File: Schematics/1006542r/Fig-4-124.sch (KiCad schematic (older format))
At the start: 15 parts, among them J1 ConnectorGeneric, U601 D3NOR-+3VDC-0VDC-nd1021041-A_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, U602 D3NOR-+3VDC-0VDC-nd1021041-AB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, U603 D3NOR-+3VDC-0VDC-nd1021041-AB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, U604 D3NOR-+3VDC-0VDC-nd1021041-AB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, U605 D3NOR-+3VDC-0VDC-nd1021041-_B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, U606 D3NOR-+3VDC-0VDC-nd1021041-_B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, U607 D3NOR-+3VDC-0VDC-nd1021041-_B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, U608 D3NOR-+3VDC-0VDC-nd1021041-_B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, U609 D3NOR-+3VDC-0VDC-nd1021041-_B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, U610 D3NOR-+3VDC-0VDC-nd1021041-A_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, U611 D3NOR-+3VDC-0VDC-nd1021041-_B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, U612 D3NOR-NC-0VDC-expander-nd1021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, U613 D3NOR-+3VDC-0VDC-nd1021041-_B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, U614 D3NOR-+3VDC-0VDC-nd1021041-_B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

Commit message: When I started recovering transcribed Block I schematics from document ND-1021041, there was no info available to me on the pinout of the NOR-gates they used, and it didn't occur to me that any might be forthcoming, so I chose a pinout arbitrarily.  It turns out that we now have the required info (SCD 1006771), and my arbitrary choices were wrong. I've therefore updated the NOR-library generator script, the relevant NOR libraries themselves, and all of the so-far-recovered Block I schematics using those gates.  It doesn't really matter in the cosmic sense, since the real Block I schematics have become available in the meantime, so that these recovered schematics are of less interest, but it will come in handy when I eventually want to do cross-checking.  I haven't checked these updated schematics in full detail, but I've spot-checked them, and run some ERCs and netlists, and it looks good to me.
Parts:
- U601, U610: value D3NOR-+3VDC-0VDC-nd1021041-A_C-___ -> D3NOR-+3VDC-0VDC-nd1021041-1_5-___; symbol D3NOR-+3VDC-0VDC-nd1021041:D3NOR-+3VDC-0VDC-nd1021041-A_C-___ -> D3NOR-+3VDC-0VDC-nd1021041:D3NOR-+3VDC-0VDC-nd1021041-1_5-___
- U602, U603, U604: value D3NOR-+3VDC-0VDC-nd1021041-ABC-___ -> D3NOR-+3VDC-0VDC-nd1021041-135-___; symbol D3NOR-+3VDC-0VDC-nd1021041:D3NOR-+3VDC-0VDC-nd1021041-ABC-___ -> D3NOR-+3VDC-0VDC-nd1021041:D3NOR-+3VDC-0VDC-nd1021041-135-___
- U605, U606, U607, U608, U609, U611, U613, U614: value D3NOR-+3VDC-0VDC-nd1021041-_B_-___ -> D3NOR-+3VDC-0VDC-nd1021041-_3_-___; symbol D3NOR-+3VDC-0VDC-nd1021041:D3NOR-+3VDC-0VDC-nd1021041-_B_-___ -> D3NOR-+3VDC-0VDC-nd1021041:D3NOR-+3VDC-0VDC-nd1021041-_3_-___
- U612: value D3NOR-NC-0VDC-expander-nd1021041-A_C-___ -> D3NOR-NC-0VDC-expander-nd1021041-1_5-___; symbol D3NOR-NC-0VDC-expander-nd1021041:D3NOR-NC-0VDC-expander-nd1021041-A_C-___ -> D3NOR-NC-0VDC-expander-nd1021041:D3NOR-NC-0VDC-expander-nd1021041-1_5-___
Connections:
- net +3VDC: now also U601.8 (+3VDC), U602.8 (+3VDC), U603.8 (+3VDC), U604.8 (+3VDC), U605.8 (+3VDC), U606.8 (+3VDC), U607.8 (+3VDC), U608.8 (+3VDC), U609.8 (+3VDC), U610.8 (+3VDC), U611.8 (+3VDC), U613.8 (+3VDC), U614.8 (+3VDC); no longer U601.6 (+3VDC), U602.6 (+3VDC), U603.6 (+3VDC), U604.6 (+3VDC), U605.6 (+3VDC), U606.6 (+3VDC), U607.6 (+3VDC), U608.6 (+3VDC), U609.6 (+3VDC), U610.6 (+3VDC), U611.6 (+3VDC), U613.6 (+3VDC), U614.6 (+3VDC)
- net 0VDC: now also U601.4 (0VDC), U602.4 (0VDC), U603.4 (0VDC), U604.4 (0VDC), U605.1 (0VDC), U606.1 (0VDC), U607.1 (0VDC), U608.1 (0VDC), U609.1 (0VDC), U610.4 (0VDC), U611.1 (0VDC), U612.4 (0VDC), U613.1 (0VDC), U614.1 (0VDC); no longer U601.5 (0VDC), U602.5 (0VDC), U603.5 (0VDC), U604.5 (0VDC), U605.2 (0VDC), U606.2 (0VDC), U607.2 (0VDC), U608.2 (0VDC), U609.2 (0VDC), U610.5 (0VDC), U611.2 (0VDC), U612.5 (0VDC), U613.2 (0VDC), U614.2 (0VDC)
- net PIN51: now also U602.1; no longer U602.4 (A)
- net PIN57: now also U612.5; no longer U612.2 (C)
- net PIN63: now also U610.5; no longer U610.2 (C)
- net at J1.49: now also U611.7; no longer U611.1 (J)
- net at J1.69: now also U601.1; no longer U601.4 (A)
- net at J1.55: now also U609.7; no longer U609.1 (J)
- net at U604.1: now also J1.61, U602.5, U603.5, U610.1; no longer U609.3 (B)
- net at U605.3: now also U602.7; no longer U602.1 (J)
- net at U611.3, U613.3, U614.3: now also U605.7; no longer U605.1 (J)
- net at J1.59: now also U608.7; no longer U608.1 (J)
- net at J1.73: now also U603.1; no longer U603.4 (A)
- net at J1.75: now also U601.5; no longer U601.2 (C)
- net at U606.3, U607.3, U608.3: now also U603.7; no longer U603.1 (J)
- new net: J1.83, U606.7, U607.7
- new net: J1.43, U613.7, U614.7
- new net: U604.7, U609.3
- new net: J1.53, U610.7, U612.7
- new net: U601.7, U604.5, U612.1
- now unconnected: U602.2 (C), U603.2 (C), U604.2 (C)
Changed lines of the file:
@@
 $EndComp
 $Comp
-L D3NOR-+3VDC-0VDC-nd1021041:D3NOR-+3VDC-0VDC-nd1021041-_B_-___ U609
+L D3NOR-+3VDC-0VDC-nd1021041:D3NOR-+3VDC-0VDC-nd1021041-_3_-___ U609
 U 1 1 5BF978FA
 P 13050 7300
 F 0 "U609" H 13050 7625 140 0001 C CNB
-F 1 "D3NOR-+3VDC-0VDC-nd1021041-_B_-___" H 13050 7725 140 0001 C CNN
+F 1 "D3NOR-+3VDC-0VDC-nd1021041-_3_-___" H 13050 7725 140 0001 C CNN
 F 2 "" H 13050 7775 140 0001 C CNN
 F 3 "" H 13050 7775 140 0001 C CNN
@@
 $EndComp
 $Comp
-L D3NOR-+3VDC-0VDC-nd1021041:D3NOR-+3VDC-0VDC-nd1021041-A_C-___ U610
+L D3NOR-+3VDC-0VDC-nd1021041:D3NOR-+3VDC-0VDC-nd1021041-1_5-___ U610
 U 1 1 5BF978FB
 P 13050 8500
 F 0 "U610" H 13050 8825 140 0001 C CNB
-F 1 "D3NOR-+3VDC-0VDC-nd1021041-A_C-___" H 13050 8925 140 0001 C CNN
+F 1 "D3NOR-+3VDC-0VDC-nd1021041-1_5-___" H 13050 8925 140 0001 C CNN
 F 2 "" H 13050 8975 140 0001 C CNN
 F 3 "" H 13050 8975 140 0001 C CNN
@@
 $EndComp
 $Comp
-L D3NOR-NC-0VDC-expander-nd1021041:D3NOR-NC-0VDC-expander-nd1021041-A_C-___ U612
+L D3NOR-NC-0VDC-expander-nd1021041:D3NOR-NC-0VDC-expander-nd1021041-1_5-___ U612
 U 1 1 5BF978FC
 P 13100 9500
 F 0 "U612" H 13100 9825 140 0001 C CNB
-F 1 "D3NOR-NC-0VDC-expander-nd1021041-A_C-___" H 13100 9925 140 0001 C CNN
+F 1 "D3NOR-NC-0VDC-expander-nd1021041-1_5-___" H 13100 9925 140 0001 C CNN
 F 2 "" H 13100 9975 140 0001 C CNN
 F 3 "" H 13100 9975 140 0001 C CNN
@@
 $EndComp
 $Comp
-L D3NOR-+3VDC-0VDC-nd1021041:D3NOR-+3VDC-0VDC-nd1021041-ABC-___ U602
+L D3NOR-+3VDC-0VDC-nd1021041:D3NOR-+3VDC-0VDC-nd1021041-135-___ U602
 U 1 1 5BF978FD
 P 7350 11675
 F 0 "U602" H 7350 12000 140 0001 C CNB
-F 1 "D3NOR-+3VDC-0VDC-nd1021041-ABC-___" H 7350 12100 140 0001 C CNN
+F 1 "D3NOR-+3VDC-0VDC-nd1021041-135-___" H 7350 12100 140 0001 C CNN
 F 2 "" H 7350 12150 140 0001 C CNN
 F 3 "" H 7350 12150 140 0001 C CNN
@@
 $EndComp
 $Comp
-L D3NOR-+3VDC-0VDC-nd1021041:D3NOR-+3VDC-0VDC-nd1021041-_B_-___ U605
+L D3NOR-+3VDC-0VDC-nd1021041:D3NOR-+3VDC-0VDC-nd1021041-_3_-___ U605
 U 1 1 5BF978FE
 P 10225 11675
 F 0 "U605" H 10225 12000 140 0001 C CNB
-F 1 "D3NOR-+3VDC-0VDC-nd1021041-_B_-___" H 10225 12100 140 0001 C CNN
+F 1 "D3NOR-+3VDC-0VDC-nd1021041-_3_-___" H 10225 12100 140 0001 C CNN
 F 2 "" H 10225 12150 140 0001 C CNN
 F 3 "" H 10225 12150 140 0001 C CNN
@@
 $EndComp
 $Comp
-L D3NOR-+3VDC-0VDC-nd1021041:D3NOR-+3VDC-0VDC-nd1021041-_B_-___ U611
+L D3NOR-+3VDC-0VDC-nd1021041:D3NOR-+3VDC-0VDC-nd1021041-_3_-___ U611
 U 1 1 5BF978FF
 P 13075 10475
 F 0 "U611" H 13075 10800 140 0001 C CNB
-F 1 "D3NOR-+3VDC-0VDC-nd1021041-_B_-___" H 13075 10900 140 0001 C CNN
+F 1 "D3NOR-+3VDC-0VDC-nd1021041-_3_-___" H 13075 10900 140 0001 C CNN
 F 2 "" H 13075 10950 140 0001 C CNN
 F 3 "" H 13075 10950 140 0001 C CNN
@@
 $EndComp
 $Comp
-L D3NOR-+3VDC-0VDC-nd1021041:D3NOR-+3VDC-0VDC-nd1021041-_B_-___ U613
+L D3NOR-+3VDC-0VDC-nd1021041:D3NOR-+3VDC-0VDC-nd1021041-_3_-___ U613
 U 1 1 5BF97900
 P 13125 11675
 F 0 "U613" H 13125 12000 140 0001 C CNB
-F 1 "D3NOR-+3VDC-0VDC-nd1021041-_B_-___" H 13125 12100 140 0001 C CNN
+F 1 "D3NOR-+3VDC-0VDC-nd1021041-_3_-___" H 13125 12100 140 0001 C CNN
 F 2 "" H 13125 12150 140 0001 C CNN
 F 3 "" H 13125 12150 140 0001 C CNN
@@
 $EndComp
 $Comp
-L D3NOR-+3VDC-0VDC-nd1021041:D3NOR-+3VDC-0VDC-nd1021041-_B_-___ U614
+L D3NOR-+3VDC-0VDC-nd1021041:D3NOR-+3VDC-0VDC-nd1021041-_3_-___ U614
 U 1 1 5BF97901
 P 13150 12900
 F 0 "U614" H 13150 13225 140 0001 C CNB
-F 1 "D3NOR-+3VDC-0VDC-nd1021041-_B_-___" H 13150 13325 140 0001 C CNN
+F 1 "D3NOR-+3VDC-0VDC-nd1021041-_3_-___" H 13150 13325 140 0001 C CNN
 F 2 "" H 13150 13375 140 0001 C CNN
 F 3 "" H 13150 13375 140 0001 C CNN
@@
 $EndComp
 $Comp
-L D3NOR-+3VDC-0VDC-nd1021041:D3NOR-+3VDC-0VDC-nd1021041-ABC-___ U604
+L D3NOR-+3VDC-0VDC-nd1021041:D3NOR-+3VDC-0VDC-nd1021041-135-___ U604
 U 1 1 5BF9790A
 P 10150 7300
 F 0 "U604" H 10150 7625 140 0001 C CNB
-F 1 "D3NOR-+3VDC-0VDC-nd1021041-ABC-___" H 10150 7725 140 0001 C CNN
+F 1 "D3NOR-+3VDC-0VDC-nd1021041-135-___" H 10150 7725 140 0001 C CNN
 F 2 "" H 10150 7775 140 0001 C CNN
 F 3 "" H 10150 7775 140 0001 C CNN
@@
 $EndComp
 $Comp
-L D3NOR-+3VDC-0VDC-nd1021041:D3NOR-+3VDC-0VDC-nd1021041-A_C-___ U601
+L D3NOR-+3VDC-0VDC-nd1021041:D3NOR-+3VDC-0VDC-nd1021041-1_5-___ U601
 U 1 1 5BF9790B
 P 7225 7650
 F 0 "U601" H 7225 7975 140 0001 C CNB
-F 1 "D3NOR-+3VDC-0VDC-nd1021041-A_C-___" H 7225 8075 140 0001 C CNN
+F 1 "D3NOR-+3VDC-0VDC-nd1021041-1_5-___" H 7225 8075 140 0001 C CNN
 F 2 "" H 7225 8125 140 0001 C CNN
 F 3 "" H 7225 8125 140 0001 C CNN
@@
 $EndComp
 $Comp
-L D3NOR-+3VDC-0VDC-nd1021041:D3NOR-+3VDC-0VDC-nd1021041-_B_-___ U608
+L D3NOR-+3VDC-0VDC-nd1021041:D3NOR-+3VDC-0VDC-nd1021041-_3_-___ U608
 U 1 1 5BF9790C
 P 13025 6100
 F 0 "U608" H 13025 6425 140 0001 C CNB
-F 1 "D3NOR-+3VDC-0VDC-nd1021041-_B_-___" H 13025 6525 140 0001 C CNN
+F 1 "D3NOR-+3VDC-0VDC-nd1021041-_3_-___" H 13025 6525 140 0001 C CNN
 F 2 "" H 13025 6575 140 0001 C CNN
 F 3 "" H 13025 6575 140 0001 C CNN
@@
 $EndComp
 $Comp
-L D3NOR-+3VDC-0VDC-nd1021041:D3NOR-+3VDC-0VDC-nd1021041-_B_-___ U606
+L D3NOR-+3VDC-0VDC-nd1021041:D3NOR-+3VDC-0VDC-nd1021041-_3_-___ U606
 U 1 1 5BF9790D
 P 13000 4950
 F 0 "U606" H 13000 5275 140 0001 C CNB
-F 1 "D3NOR-+3VDC-0VDC-nd1021041-_B_-___" H 13000 5375 140 0001 C CNN
+F 1 "D3NOR-+3VDC-0VDC-nd1021041-_3_-___" H 13000 5375 140 0001 C CNN
 F 2 "" H 13000 5425 140 0001 C CNN
 F 3 "" H 13000 5425 140 0001 C CNN
@@
 $EndComp
 $Comp
-L D3NOR-+3VDC-0VDC-nd1021041:D3NOR-+3VDC-0VDC-nd1021041-_B_-___ U607
+L D3NOR-+3VDC-0VDC-nd1021041:D3NOR-+3VDC-0VDC-nd1021041-_3_-___ U607
 U 1 1 5BF9790E
 P 13025 3700
 F 0 "U607" H 13025 4025 140 0001 C CNB
-F 1 "D3NOR-+3VDC-0VDC-nd1021041-_B_-___" H 13025 4125 140 0001 C CNN
+F 1 "D3NOR-+3VDC-0VDC-nd1021041-_3_-___" H 13025 4125 140 0001 C CNN
 F 2 "" H 13025 4175 140 0001 C CNN
 F 3 "" H 13025 4175 140 0001 C CNN
@@
 $EndComp
 $Comp
-L D3NOR-+3VDC-0VDC-nd1021041:D3NOR-+3VDC-0VDC-nd1021041-ABC-___ U603
+L D3NOR-+3VDC-0VDC-nd1021041:D3NOR-+3VDC-0VDC-nd1021041-135-___ U603
 U 1 1 5BF9790F
 P 10100 4950
 F 0 "U603" H 10100 5275 140 0001 C CNB
-F 1 "D3NOR-+3VDC-0VDC-nd1021041-ABC-___" H 10100 5375 140 0001 C CNN
+F 1 "D3NOR-+3VDC-0VDC-nd1021041-135-___" H 10100 5375 140 0001 C CNN
 F 2 "" H 10100 5425 140 0001 C CNN
 F 3 "" H 10100 5425 140 0001 C CNN

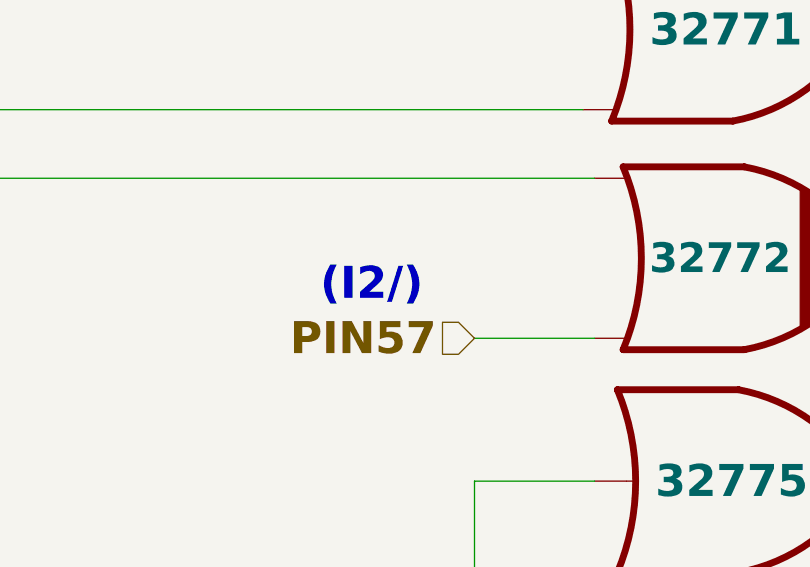
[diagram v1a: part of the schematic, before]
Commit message: Drawing 1006542- (schematic for Block I AGC module A18) has been transcribed and cross-checked/corrected vs 1006542r (derived from ND-1021041).  There are unresolved discrepancies between the two leading me to believe that there is a later, unavailable revision of the schematic drawing.  The write-up in README.md provides an analysis of all discrepancies.
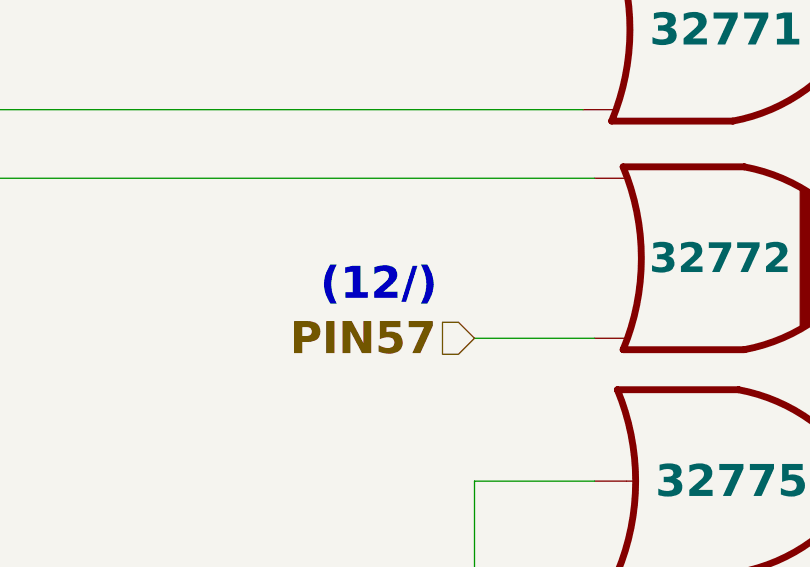
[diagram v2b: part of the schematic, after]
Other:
- note added: "(12/)"
- note removed: "(I2/)"
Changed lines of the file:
@@
 PIN57
 Text Notes 11275 9700 0    140  ~ 28
-(I2/)
+(12/)
 Text HLabel 8625 7300 0    140  Input ~ 28
 PIN63

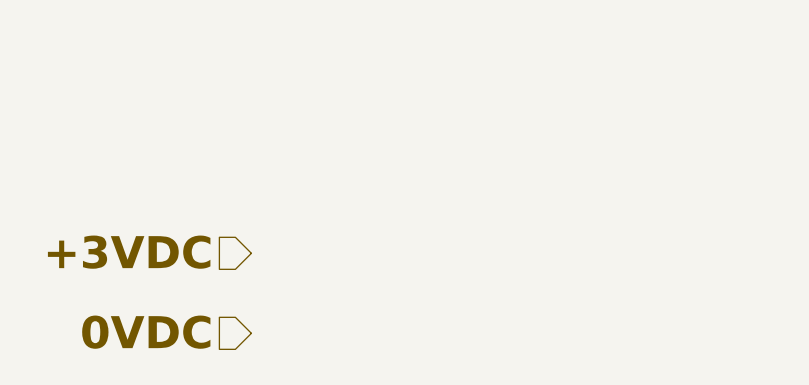
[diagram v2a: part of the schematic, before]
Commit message: Made visual changes with eelint, and other changes which should not affect the netlist to appease new features in KiCad ERC.  Unfortunately, it still does not pass ERC (due to current KiCad bugs, I believe), and it isn't possible to compare before vs after netlists because the netlist was not previously saved in the repository.  That has been correct on a go-forward basis, however.
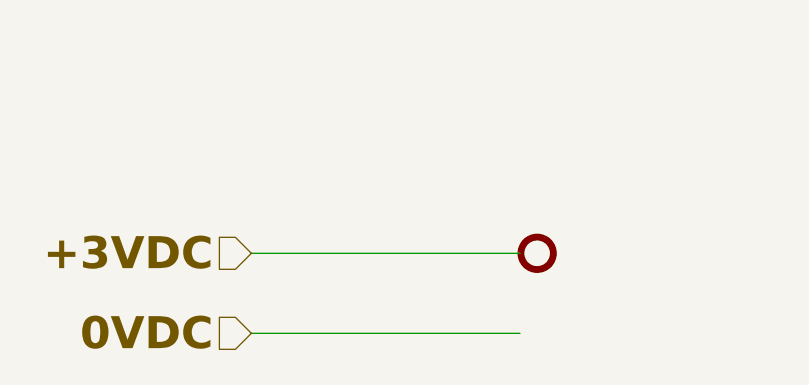
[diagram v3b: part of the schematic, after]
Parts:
- added N601, N602: Node2, symbol AGC_DSKY:Node2
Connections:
- net +3VDC: now also N601.1
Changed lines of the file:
@@
-EESchema Schematic File Version 4
+EESchema Schematic File Version 5
 LIBS:module-cache
 EELAYER 29 0
@@
 Text Notes 7875 7175 0    140  ~ 28
 (CA1/)
+$Comp
+L AGC_DSKY:Node2 N?
+U 1 1 5CBB2CE9
+P 2850 15750
+AR Path="/5BEFD1AD/5CBB2CE9" Ref="N?"  Part="1"
+AR Path="/5F3216C6/5CBB2CE9" Ref="N601"  Part="1"
+F 0 "N601" H 2850 15850 50  0001 C CNN
+F 1 "Node2" H 2850 15925 50  0001 C CNN
+F 2 "" H 2850 15750 50  0001 C CNN
+F 3 "" H 2850 15750 50  0001 C CNN
+F 4 "+3VDC" H 2775 15750 140 0001 R CNB "Caption"
+	1    2850 15750
+	-1   0    0    1
+$EndComp
+$Comp
+L AGC_DSKY:Node2 N?
+U 1 0 5CBB2CF2
+P 2850 16100
+AR Path="/5BEFD1AD/5CBB2CF2" Ref="N?"  Part="1"
+AR Path="/5F3216C6/5CBB2CF2" Ref="N602"  Part="1"
+F 0 "N602" H 2850 16200 50  0001 C CNN
+F 1 "Node2" H 2850 16275 50  0001 C CNN
+F 2 "" H 2850 16100 50  0001 C CNN
+F 3 "" H 2850 16100 50  0001 C CNN
+F 4 "0VDC" H 2775 16100 140 0001 R CNB "Caption"
+	1    2850 16100
+	-1   0    0    1
+$EndComp
+Wire Wire Line
+	1600 15750 2775 15750
+Wire Wire Line
+	1600 16100 2775 16100
 $EndSCHEMATC
